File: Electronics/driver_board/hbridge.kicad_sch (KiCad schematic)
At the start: 33 parts, among them J2 Conn_01x02, Q1 IAUZ40N10S5N130, Q2 IAUZ40N10S5N130, Q3 IAUZ40N10S5N130, Q4 IAUZ40N10S5N130, U2 UCC27302ADRCR, U3 UCC27302ADRCR, U4 INA241A2xDDF

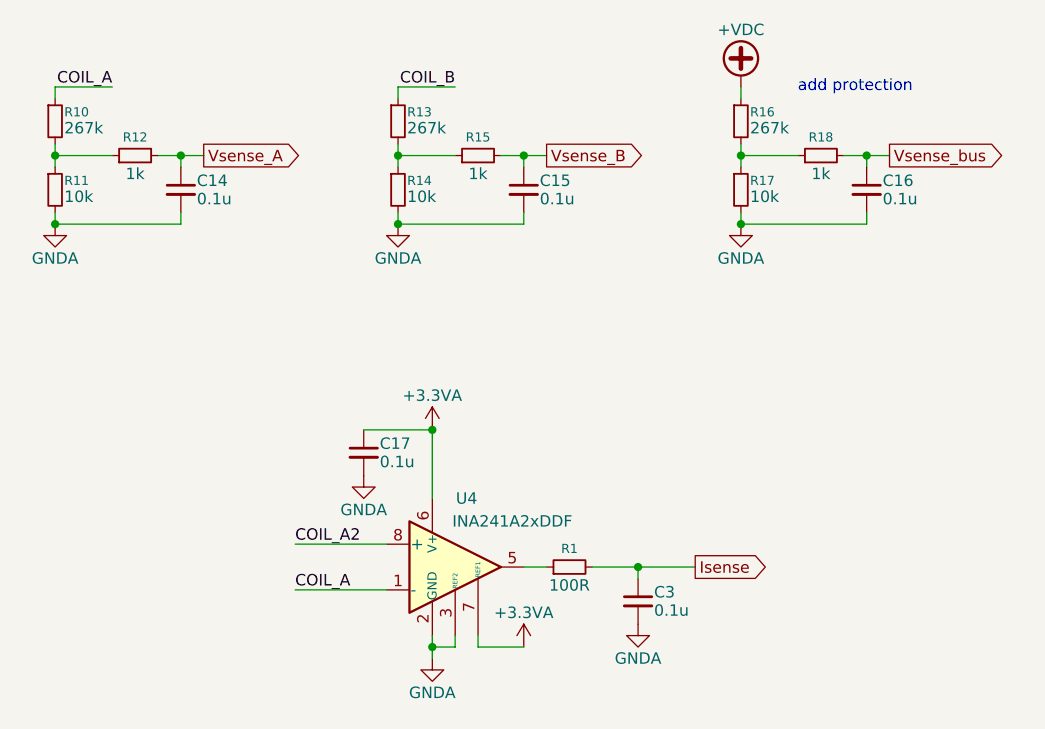
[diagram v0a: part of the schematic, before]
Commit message: [pcb] Added regulators, pin mapping
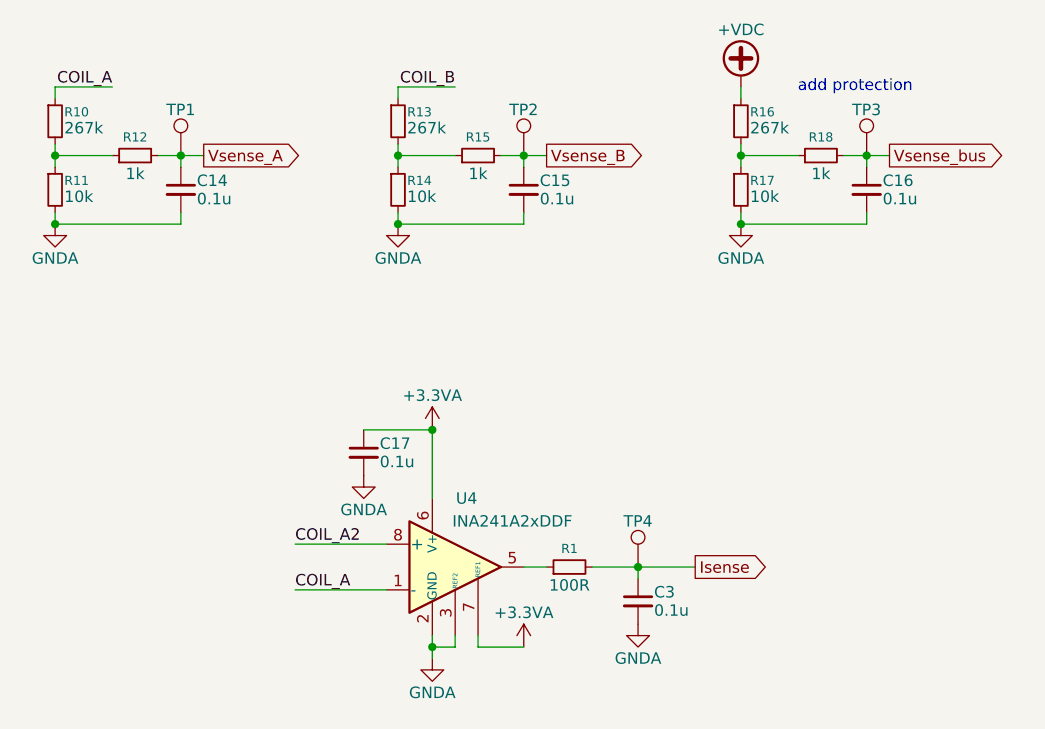
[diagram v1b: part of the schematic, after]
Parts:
- added TP1, TP2, TP3, TP4: TestPoint, Connector_PinHeader_1.00mm:PinHeader_1x01_P1.00mm_Vertical, symbol Connector:TestPoint
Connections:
- net Isense: now also TP4.1
- net Vsense_A: now also TP1.1
- net Vsense_B: now also TP2.1
- net Vsense_bus: now also TP3.1

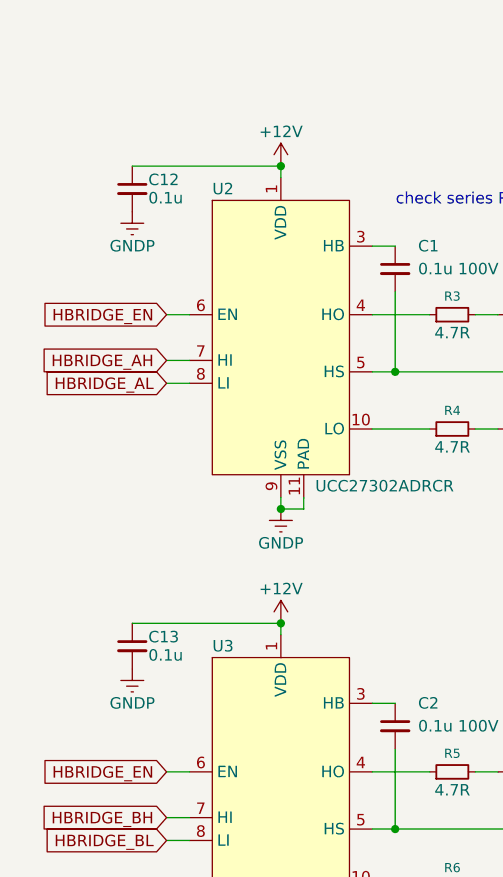
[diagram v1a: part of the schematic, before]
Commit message: [pcb] Populating efuse parts
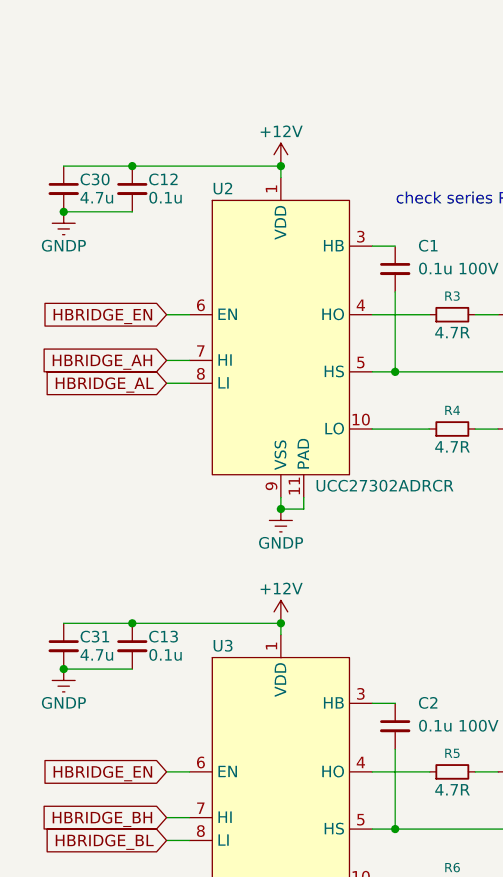
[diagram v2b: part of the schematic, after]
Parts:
- added C30, C31: 4.7u, symbol Device:C_Small
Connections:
- net +12V: now also C30.1, C31.1
- net GNDP: now also C30.2, C31.2
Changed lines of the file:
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@@
 	)
 	(junction
+		(at 54.61 110.49)
+		(diameter 0)
+		(color 0 0 0 0)
+	)
+	(junction
 		(at 83.82 82.55)
 		(diameter 0)
@@
 	)
 	(junction
+		(at 46.99 64.77)
+		(diameter 0)
+		(color 0 0 0 0)
+	)
+	(junction
 		(at 241.3 40.64)
 		(diameter 0)
@@
 	)
 	(junction
+		(at 54.61 59.69)
+		(diameter 0)
+		(color 0 0 0 0)
+	)
+	(junction
 		(at 71.12 59.69)
 		(diameter 0)
@@
 	)
 	(junction
+		(at 46.99 115.57)
+		(diameter 0)
+		(color 0 0 0 0)
+	)
+	(junction
 		(at 102.87 82.55)
 		(diameter 0)
@@
 	(wire
 		(pts
+			(xy 46.99 115.57) (xy 54.61 115.57)
+		)
+		(stroke
+			(width 0)
+			(type default)
+		)
+	)
+	(wire
+		(pts
 			(xy 102.87 82.55) (xy 128.27 82.55)
 		)
@@
 	(wire
 		(pts
+			(xy 46.99 110.49) (xy 54.61 110.49)
+		)
+		(stroke
+			(width 0)
+			(type default)
+		)
+	)
+	(wire
+		(pts
 			(xy 165.1 33.02) (xy 171.45 33.02)
 		)
@@
 	(wire
 		(pts
+			(xy 46.99 64.77) (xy 54.61 64.77)
+		)
+		(stroke
+			(width 0)
+			(type default)
+		)
+	)
+	(wire
+		(pts
 			(xy 179.07 39.37) (xy 179.07 40.64)
 		)
@@
 	(wire
 		(pts
+			(xy 46.99 59.69) (xy 54.61 59.69)
+		)
+		(stroke
+			(width 0)
+			(type default)
+		)
+	)
+	(wire
+		(pts
 			(xy 209.55 25.4) (xy 203.2 25.4)
 		)
@@
 	)
 	(symbol
+		(lib_id "Device:C_Small")
+		(at 46.99 113.03 0)
+		(unit 1)
+		(exclude_from_sim no)
+		(in_bom yes)
+		(on_board yes)
+		(dnp no)
+		(property "Reference" "C31"
+			(at 48.768 112.014 0)
+			(effects
+				(font
+					(size 1.27 1.27)
+				)
+				(justify left)
+			)
+		)
+		(property "Value" "4.7u"
+			(at 48.768 114.046 0)
+			(effects
+				(font
+					(size 1.27 1.27)
+				)
+				(justify left)
+			)
+		)
+		(property "Footprint" ""
+			(at 46.99 113.03 0)
+			(effects
+				(font
+					(size 1.27 1.27)
+				)
+				(hide yes)
+			)
+		)
+		(property "Datasheet" "~"
+			(at 46.99 113.03 0)
+			(effects
+				(font
+					(size 1.27 1.27)
+				)
+				(hide yes)
+			)
+		)
+		(property "Description" "Unpolarized capacitor, small symbol"
+			(at 46.99 113.03 0)
+			(effects
+				(font
+					(size 1.27 1.27)
+				)
+				(hide yes)
+			)
+		)
+		(pin "1"
+		)
+		(pin "2"
+		)
+		(instances
+			(project "driver_board"
+				(path "/90d9ae7d-4001-450f-acdb-4ca976b51116/b498c85e-3d95-495c-baed-daa9b16c230d"
+					(reference "C31")
+					(unit 1)
+				)
+			)
+		)
+	)
+	(symbol
 		(lib_id "power:+3.3VA")
 		(at 217.17 87.63 0)
@@
 	)
 	(symbol
+		(lib_id "Device:C_Small")
+		(at 46.99 62.23 0)
+		(unit 1)
+		(exclude_from_sim no)
+		(in_bom yes)
+		(on_board yes)
+		(dnp no)
+		(property "Reference" "C30"
+			(at 48.768 61.214 0)
+			(effects
+				(font
+					(size 1.27 1.27)
+				)
+				(justify left)
+			)
+		)
+		(property "Value" "4.7u"
+			(at 48.768 63.246 0)
+			(effects
+				(font
+					(size 1.27 1.27)
+				)
+				(justify left)
+			)
+		)
+		(property "Footprint" ""
+			(at 46.99 62.23 0)
+			(effects
+				(font
+					(size 1.27 1.27)
+				)
+				(hide yes)
+			)
+		)
+		(property "Datasheet" "~"
+			(at 46.99 62.23 0)
+			(effects
+				(font
+					(size 1.27 1.27)
+				)
+				(hide yes)
+			)
+		)
+		(property "Description" "Unpolarized capacitor, small symbol"
+			(at 46.99 62.23 0)
+			(effects
+				(font
+					(size 1.27 1.27)
+				)
+				(hide yes)
+			)
+		)
+		(pin "1"
+		)
+		(pin "2"
+		)
+		(instances
+			(project "driver_board"
+				(path "/90d9ae7d-4001-450f-acdb-4ca976b51116/b498c85e-3d95-495c-baed-daa9b16c230d"
+					(reference "C30")
+					(unit 1)
+				)
+			)
+		)
+	)
+	(symbol
 		(lib_id "power:GND")
 		(at 58.42 148.59 0)
@@
 	(symbol
 		(lib_id "power:Earth")
-		(at 54.61 64.77 0)
+		(at 46.99 64.77 0)
 		(unit 1)
 		(exclude_from_sim no)
@@
 		(dnp no)
 		(property "Reference" "#PWR041"
-			(at 54.61 71.12 0)
+			(at 46.99 71.12 0)
 			(effects
 				(font
@@
 		)
 		(property "Value" "GNDP"
-			(at 54.61 68.58 0)
+			(at 46.99 68.58 0)
 			(effects
 				(font
@@
 		)
 		(property "Footprint" ""
-			(at 54.61 64.77 0)
+			(at 46.99 64.77 0)
 			(effects
 				(font
@@
 		)
 		(property "Datasheet" "~"
-			(at 54.61 64.77 0)
+			(at 46.99 64.77 0)
 			(effects
 				(font
@@
 		)
 		(property "Description" "Power symbol creates a global label with name \"Earth\""
-			(at 54.61 64.77 0)
+			(at 46.99 64.77 0)
 			(effects
 				(font
@@
 	(symbol
 		(lib_id "power:Earth")
-		(at 54.61 115.57 0)
+		(at 46.99 115.57 0)
 		(unit 1)
 		(exclude_from_sim no)
@@
 		(dnp no)
 		(property "Reference" "#PWR042"
-			(at 54.61 121.92 0)
+			(at 46.99 121.92 0)
 			(effects
 				(font
@@
 		)
 		(property "Value" "GNDP"
-			(at 54.61 119.38 0)
+			(at 46.99 119.38 0)
 			(effects
 				(font
@@
 		)
 		(property "Footprint" ""
-			(at 54.61 115.57 0)
+			(at 46.99 115.57 0)
 			(effects
 				(font
@@
 		)
 		(property "Datasheet" "~"
-			(at 54.61 115.57 0)
+			(at 46.99 115.57 0)
 			(effects
 				(font
@@
 		)
 		(property "Description" "Power symbol creates a global label with name \"Earth\""
-			(at 54.61 115.57 0)
+			(at 46.99 115.57 0)
 			(effects
 				(font

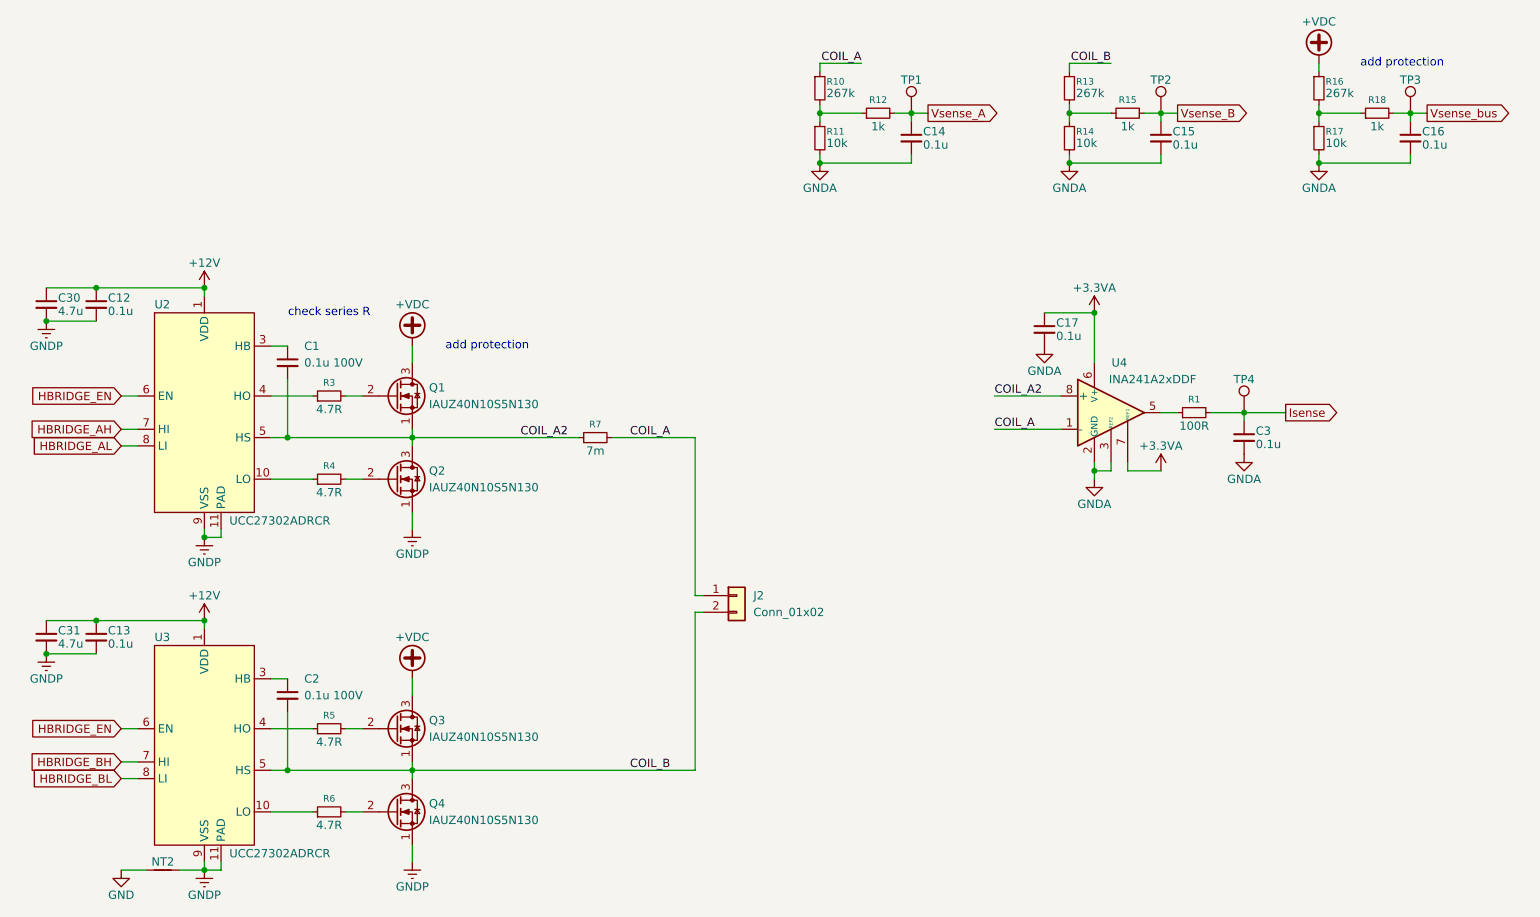
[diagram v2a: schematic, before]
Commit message: Added TVS diodes, bulk capacitors
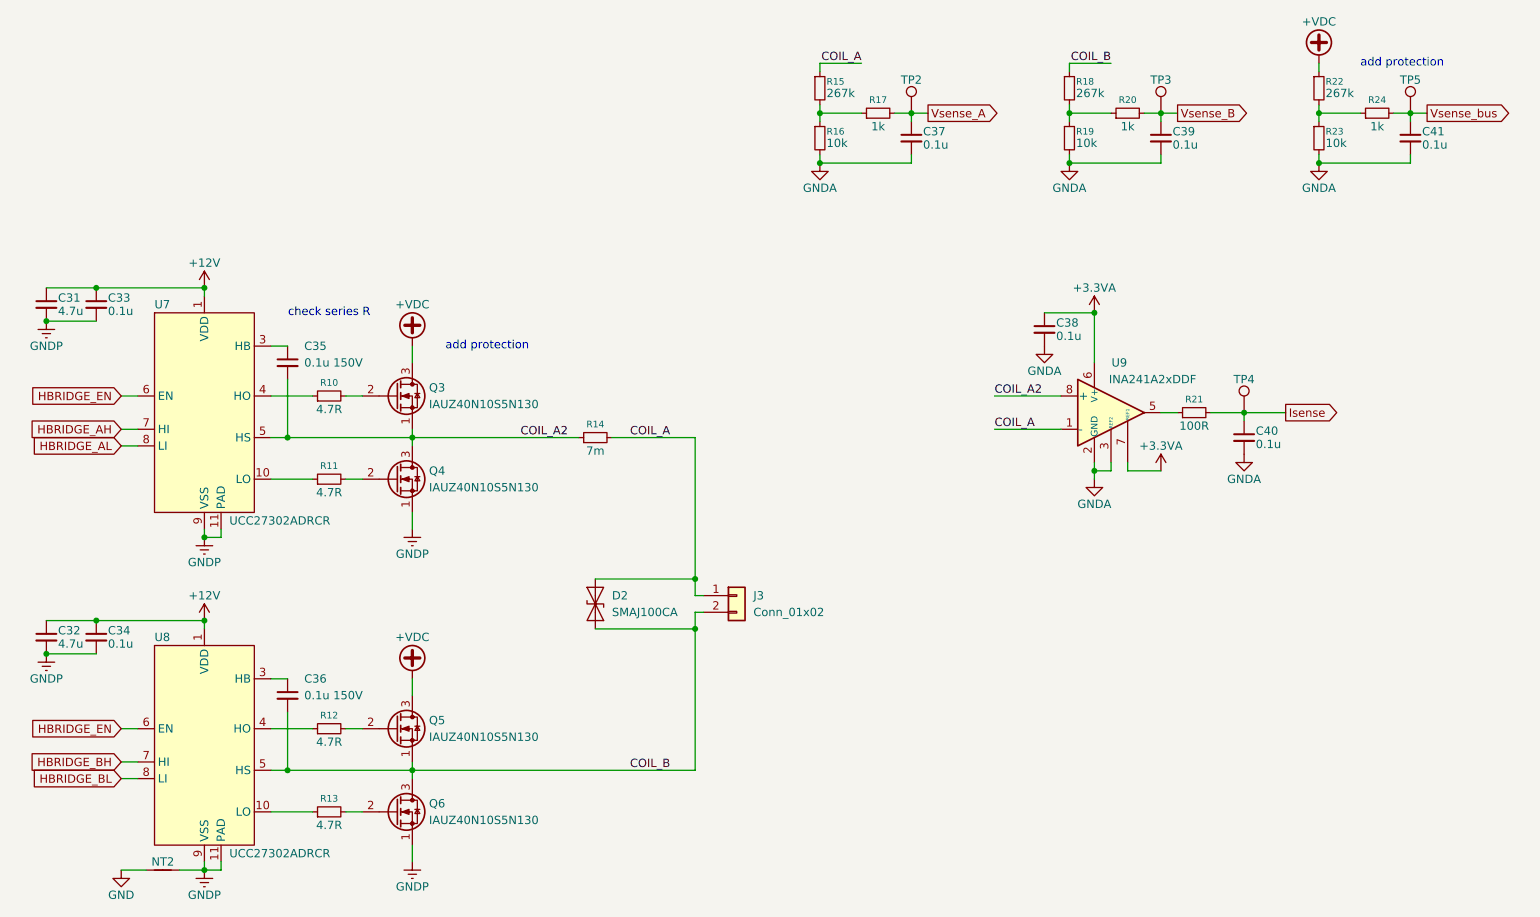
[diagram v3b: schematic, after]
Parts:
- added D2: SMAJ100CA, Diode_SMD:D_SMA, symbol Diode:SMAJ100CA
- C31: renamed from C30; footprint (none) -> Capacitor_SMD:C_0603_1608Metric
- C32: renamed from C31; footprint (none) -> Capacitor_SMD:C_0603_1608Metric
- C33: renamed from C12; footprint (none) -> Capacitor_SMD:C_0402_1005Metric
- C34: renamed from C13; footprint (none) -> Capacitor_SMD:C_0402_1005Metric
- C35: renamed from C1; value 0.1u 100V -> 0.1u 150V; footprint (none) -> Capacitor_SMD:C_0805_2012Metric; MPN (none) -> CC0805KKX7RYBB104
- C36: renamed from C2; value 0.1u 100V -> 0.1u 150V; footprint (none) -> Capacitor_SMD:C_0805_2012Metric; MPN (none) -> CC0805KKX7RYBB104
- C37: renamed from C14; footprint (none) -> Capacitor_SMD:C_0402_1005Metric
- C38: renamed from C17; footprint (none) -> Capacitor_SMD:C_0402_1005Metric
- C39: renamed from C15; footprint (none) -> Capacitor_SMD:C_0402_1005Metric
- C40: renamed from C3; footprint (none) -> Capacitor_SMD:C_0402_1005Metric
- C41: renamed from C16; footprint (none) -> Capacitor_SMD:C_0402_1005Metric
- R10: renamed from R3; footprint (none) -> Resistor_SMD:R_0805_2012Metric
- R11: renamed from R4; footprint (none) -> Resistor_SMD:R_0805_2012Metric
- R12: renamed from R5; footprint (none) -> Resistor_SMD:R_0805_2012Metric
- R13: renamed from R6; footprint (none) -> Resistor_SMD:R_0805_2012Metric
- R15: renamed from R10; footprint (none) -> Resistor_SMD:R_0603_1608Metric
- R16: renamed from R11; footprint (none) -> Resistor_SMD:R_0603_1608Metric
- R17: renamed from R12; footprint (none) -> Resistor_SMD:R_0603_1608Metric
- R18: renamed from R13; footprint (none) -> Resistor_SMD:R_0603_1608Metric
- R19: renamed from R14; footprint (none) -> Resistor_SMD:R_0603_1608Metric
- R20: renamed from R15; footprint (none) -> Resistor_SMD:R_0603_1608Metric
- R21: renamed from R1; footprint (none) -> Resistor_SMD:R_0603_1608Metric
- R22: renamed from R16; footprint (none) -> Resistor_SMD:R_0603_1608Metric
- R23: renamed from R17; footprint (none) -> Resistor_SMD:R_0603_1608Metric
- R24: renamed from R18; footprint (none) -> Resistor_SMD:R_0603_1608Metric
- renumbered J2 to J3, Q1 to Q3, Q2 to Q4, Q3 to Q5, Q4 to Q6, R7 to R14, TP1 to TP2, TP2 to TP3, TP3 to TP5, U2 to U7, U3 to U8, U4 to U9
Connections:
- net COIL_A: now also D2.2 (A2)
- net COIL_B: now also D2.1 (A1)

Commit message: Initial PCB configuration
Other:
- note added: "add capacitors"
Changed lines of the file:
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@@
 		(company "D. Watman")
 	)
-	(text "add protection"
+	(text "add capacitors"
 		(exclude_from_sim no)
 		(at 114.3 68.58 0)

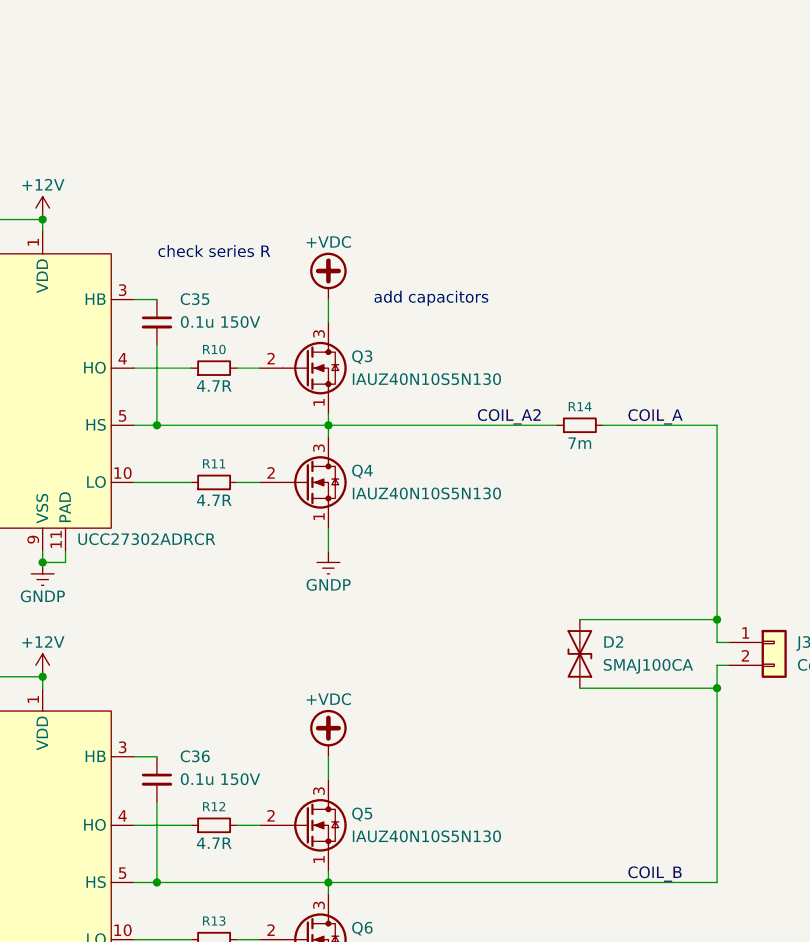
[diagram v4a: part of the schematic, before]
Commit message: Added more capacitors, part numbers.
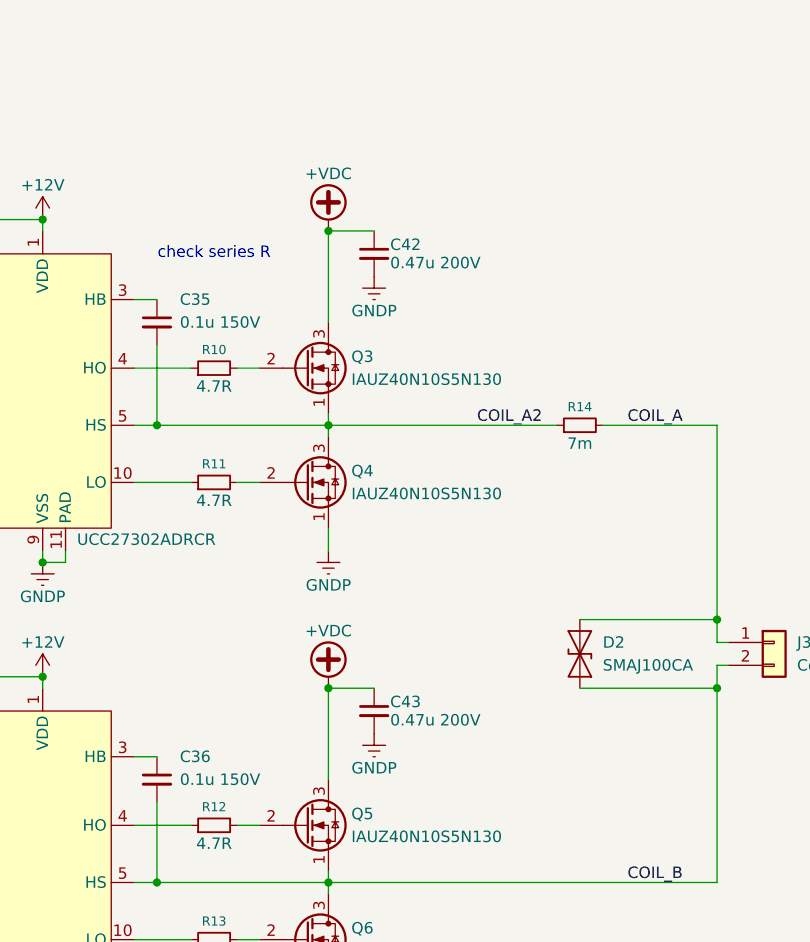
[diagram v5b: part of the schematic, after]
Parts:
- added C42, C43: 0.47u 200V, Capacitor_SMD:C_1210_3225Metric, symbol Device:C_Small
- R10, R11, R12, R13: footprint Resistor_SMD:R_0805_2012Metric -> Resistor_SMD:R_0603_1608Metric; MPN (none) -> RCS06034R70FKEA
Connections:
- net +VDC: now also C42.1, C43.1
- net GNDP: now also C42.2, C43.2
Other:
- note removed: "add capacitors"
